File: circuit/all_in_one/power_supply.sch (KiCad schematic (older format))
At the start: 22 parts

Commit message: [All in one]Construct mode circuits
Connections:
- net at D?.2 (A), Q?.2 (D): now also L?.2
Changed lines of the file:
@@
 	3200 2500 3200 2250
 Wire Wire Line
-	2500 2500 4000 2500
+	2500 2500 2750 2500
+Wire Wire Line
+	2750 2500 3200 2500
+Wire Wire Line
+	3200 2500 3600 2500
+Wire Wire Line
+	3600 2500 4000 2500
 Wire Wire Line
 	4000 2500 4000 2250
@@
 	4000 1700 4450 1700
 Wire Wire Line
-	2500 1700 3200 1700
+	2500 1700 2700 1700
+Wire Wire Line
+	2700 1700 3200 1700
 Connection ~ 3200 2500
 Wire Wire Line
@@
 $EndComp
 Wire Wire Line
-	3550 3950 5550 3950
+	3550 3950 3900 3950
+Wire Wire Line
+	3900 3950 5050 3950
+Wire Wire Line
+	5050 3950 5250 3950
+Wire Wire Line
+	5250 3950 5550 3950
 Wire Wire Line
 	3550 3950 3550 4150
@@
 	5400 3750 2900 3750
 Wire Wire Line
-	2900 3750 2900 4750
+	2900 3750 2900 3950
+Wire Wire Line
+	2900 3950 2900 4750
 Text HLabel 2550 3950 0    98   Input ~ 0
 12V
@@
 GND
 Wire Wire Line
-	2550 3950 3250 3950
+	2550 3950 2900 3950
+Wire Wire Line
+	2900 3950 3250 3950
 Connection ~ 2900 3950
 Wire Wire Line
@@
 Connection ~ 2900 6000
 Wire Wire Line
-	2550 6000 8200 6000
+	2550 6000 2900 6000
+Wire Wire Line
+	2900 6000 3350 6000
+Wire Wire Line
+	3350 6000 3650 6000
+Wire Wire Line
+	3650 6000 3900 6000
+Wire Wire Line
+	3900 6000 6050 6000
+Wire Wire Line
+	6050 6000 6500 6000
+Wire Wire Line
+	6500 6000 7200 6000
+Wire Wire Line
+	7200 6000 7600 6000
+Wire Wire Line
+	7600 6000 8200 6000
 Wire Wire Line
 	3900 5250 3900 6000
@@
 	3350 5100 3350 5050
 Wire Wire Line
-	3650 4850 3650 5500
+	3650 4850 3650 5450
+Wire Wire Line
+	3650 5450 3650 5500
 Wire Wire Line
 	3650 4850 3900 4850
@@
 	5600 4700 5600 5450
 Wire Wire Line
-	3650 5450 5750 5450
+	3650 5450 5600 5450
+Wire Wire Line
+	5600 5450 5750 5450
 Wire Wire Line
 	6050 6000 6050 5650
@@
 Connection ~ 6050 6000
 Wire Wire Line
-	5800 3950 6700 3950
+	5750 3950 6500 3950
+Wire Wire Line
+	6500 3950 6700 3950
 Wire Wire Line
 	6500 3950 6500 4500
 Wire Wire Line
-	5900 4700 6200 4700
+	5900 4700 6050 4700
+Wire Wire Line
+	6050 4700 6200 4700
 Wire Wire Line
 	6050 5250 6050 4700
@@
 	7200 4250 7200 3950
 Wire Wire Line
-	7000 3950 7800 3950
-Wire Wire Line
-	7200 4550 7200 5200
+	7000 3950 7200 3950
+Wire Wire Line
+	7200 3950 7600 3950
+Wire Wire Line
+	7600 3950 7800 3950
+Wire Wire Line
+	7200 4550 7200 4850
+Wire Wire Line
+	7200 4850 7200 5200
 Wire Wire Line
 	7200 6000 7200 5500
@@
 Connection ~ 7600 3950
 Wire Wire Line
-	8000 3950 8500 3950
+	8000 3950 8200 3950
+Wire Wire Line
+	8200 3950 8500 3950
 Wire Wire Line
 	8200 3950 8200 4700

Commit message: [All in one circuit]Add DS1307
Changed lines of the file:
@@
 	3200 2500 3200 2250
 Wire Wire Line
-	2500 2500 2750 2500
-Wire Wire Line
-	2750 2500 3200 2500
-Wire Wire Line
-	3200 2500 3600 2500
-Wire Wire Line
-	3600 2500 4000 2500
+	2500 2500 4000 2500
 Wire Wire Line
 	4000 2500 4000 2250
@@
 	4000 1700 4450 1700
 Wire Wire Line
-	2500 1700 2700 1700
-Wire Wire Line
-	2700 1700 3200 1700
+	2500 1700 3200 1700
 Connection ~ 3200 2500
 Wire Wire Line
@@
 $EndComp
 Wire Wire Line
-	3550 3950 3900 3950
-Wire Wire Line
-	3900 3950 5050 3950
-Wire Wire Line
-	5050 3950 5250 3950
-Wire Wire Line
-	5250 3950 5550 3950
+	3550 3950 5550 3950
 Wire Wire Line
 	3550 3950 3550 4150
@@
 	5400 3750 2900 3750
 Wire Wire Line
-	2900 3750 2900 3950
-Wire Wire Line
-	2900 3950 2900 4750
+	2900 3750 2900 4750
 Text HLabel 2550 3950 0    98   Input ~ 0
 12V
@@
 GND
 Wire Wire Line
-	2550 3950 2900 3950
-Wire Wire Line
-	2900 3950 3250 3950
+	2550 3950 3250 3950
 Connection ~ 2900 3950
 Wire Wire Line
@@
 Connection ~ 2900 6000
 Wire Wire Line
-	2550 6000 2900 6000
-Wire Wire Line
-	2900 6000 3350 6000
-Wire Wire Line
-	3350 6000 3650 6000
-Wire Wire Line
-	3650 6000 3900 6000
-Wire Wire Line
-	3900 6000 6050 6000
-Wire Wire Line
-	6050 6000 6500 6000
-Wire Wire Line
-	6500 6000 7200 6000
-Wire Wire Line
-	7200 6000 7600 6000
-Wire Wire Line
-	7600 6000 8200 6000
+	2550 6000 8200 6000
 Wire Wire Line
 	3900 5250 3900 6000
@@
 	3350 5100 3350 5050
 Wire Wire Line
-	3650 4850 3650 5450
-Wire Wire Line
-	3650 5450 3650 5500
+	3650 4850 3650 5500
 Wire Wire Line
 	3650 4850 3900 4850
@@
 	5600 4700 5600 5450
 Wire Wire Line
-	3650 5450 5600 5450
-Wire Wire Line
-	5600 5450 5750 5450
+	3650 5450 5750 5450
 Wire Wire Line
 	6050 6000 6050 5650
@@
 Connection ~ 6050 6000
 Wire Wire Line
-	5750 3950 6500 3950
-Wire Wire Line
-	6500 3950 6700 3950
+	5750 3950 6700 3950
 Wire Wire Line
 	6500 3950 6500 4500
 Wire Wire Line
-	5900 4700 6050 4700
-Wire Wire Line
-	6050 4700 6200 4700
+	5900 4700 6200 4700
 Wire Wire Line
 	6050 5250 6050 4700
@@
 	7200 4250 7200 3950
 Wire Wire Line
-	7000 3950 7200 3950
-Wire Wire Line
-	7200 3950 7600 3950
-Wire Wire Line
-	7600 3950 7800 3950
-Wire Wire Line
-	7200 4550 7200 4850
-Wire Wire Line
-	7200 4850 7200 5200
+	7000 3950 7800 3950
+Wire Wire Line
+	7200 4550 7200 5200
 Wire Wire Line
 	7200 6000 7200 5500
@@
 Connection ~ 7600 3950
 Wire Wire Line
-	8000 3950 8200 3950
-Wire Wire Line
-	8200 3950 8500 3950
+	8000 3950 8500 3950
 Wire Wire Line
 	8200 3950 8200 4700

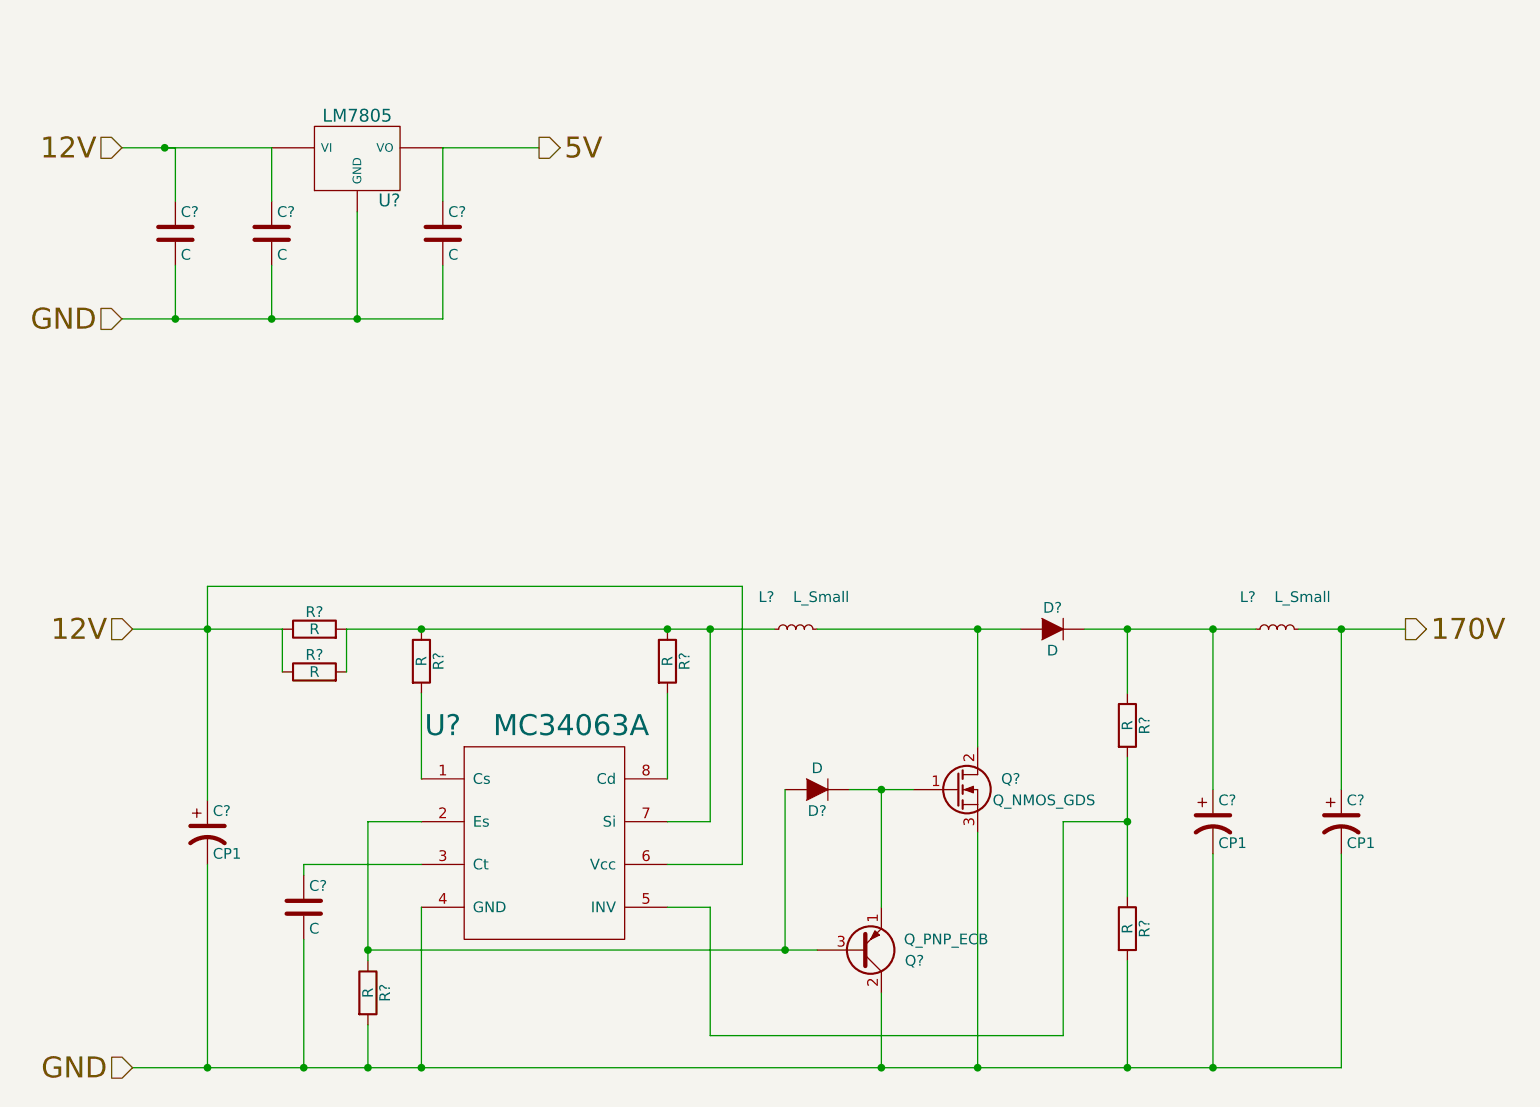
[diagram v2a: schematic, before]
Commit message: [All in one circuit]Arrange the USART pin
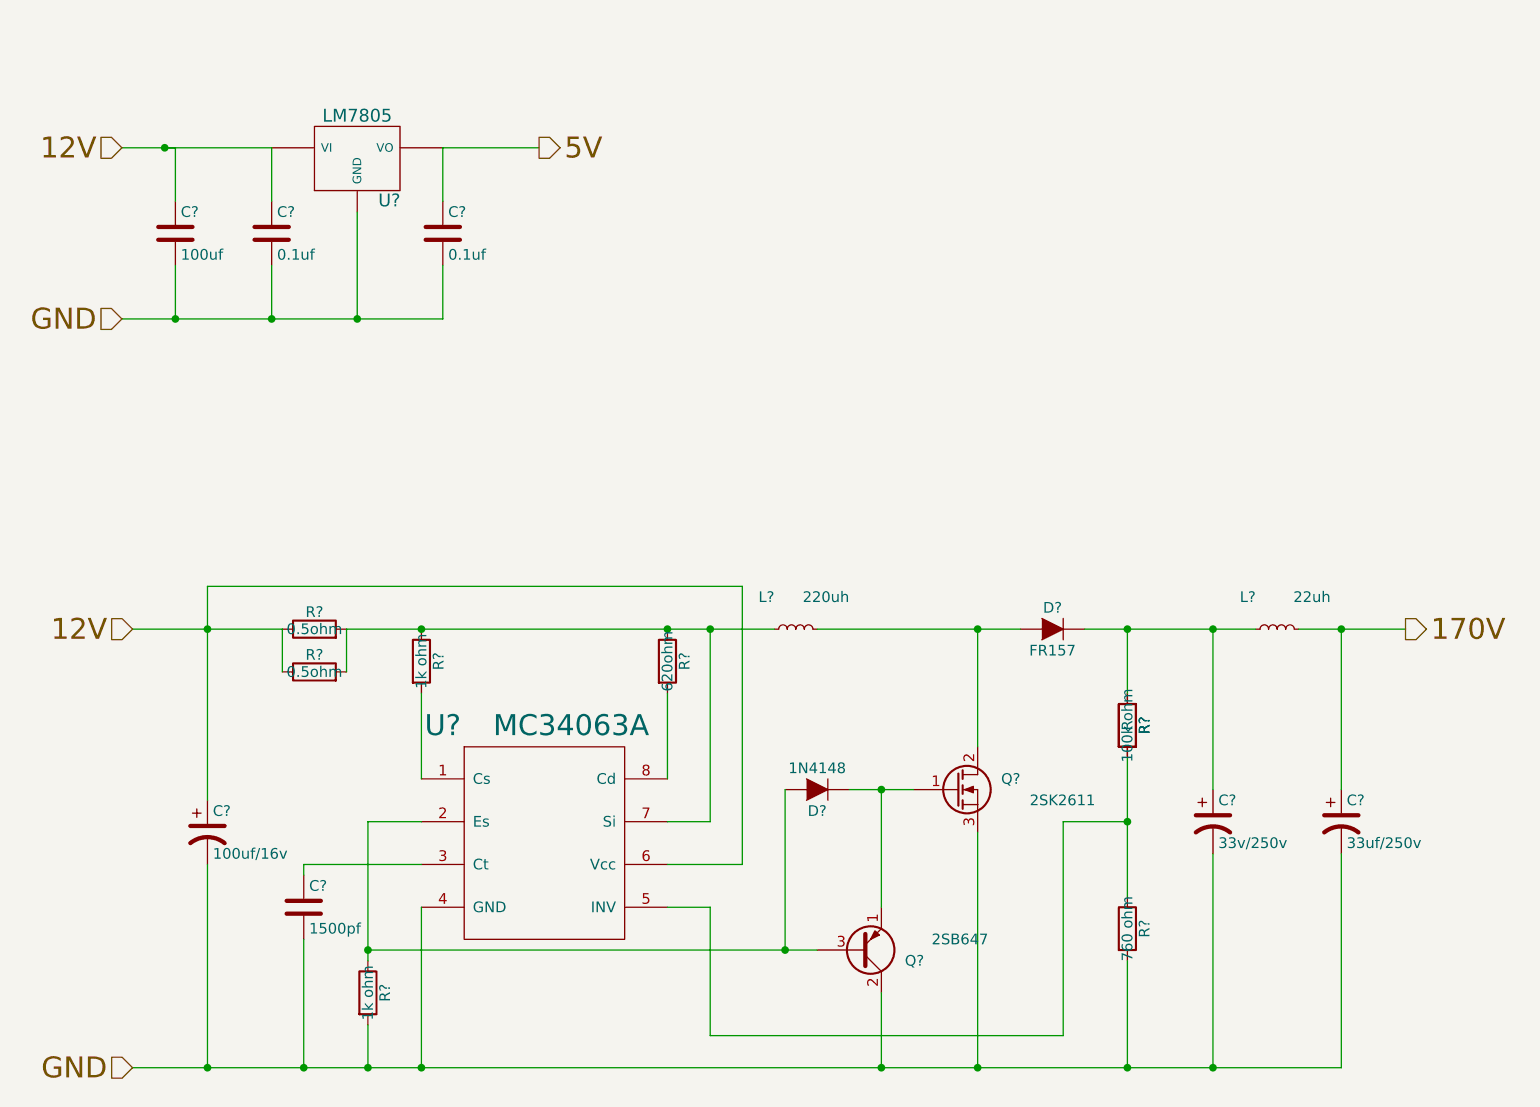
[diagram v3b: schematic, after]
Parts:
- added R?: R, symbol R
- C?: value C -> 100uf
- C? (x2): value C -> 0.1uf
- C?: value C -> 1500pf
- C?: value CP1 -> 100uf/16v
- C?: value CP1 -> 33v/250v
- C?: value CP1 -> 33uf/250v
- D?: value D -> FR157
- D?: value D -> 1N4148
- L?: value L_Small -> 220uh
- L?: value L_Small -> 22uh
- Q?: value Q_PNP_ECB -> 2SB647
- Q?: value Q_NMOS_GDS -> 2SK2611
- R? (x2): value R -> 0.5ohm
- R? (x2): value R -> 1k ohm
- R?: value R -> 620ohm
- R?: value R -> 100k ohm
- R?: value R -> 760 ohm
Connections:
- net at R?.1, R?.2, U?.5 (INV): now also R?.2
- net at C?.1, D?.1 (K), L?.1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: now also R?.1
